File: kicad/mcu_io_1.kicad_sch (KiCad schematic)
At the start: 1 part, among them U5 MCXN947VDFT

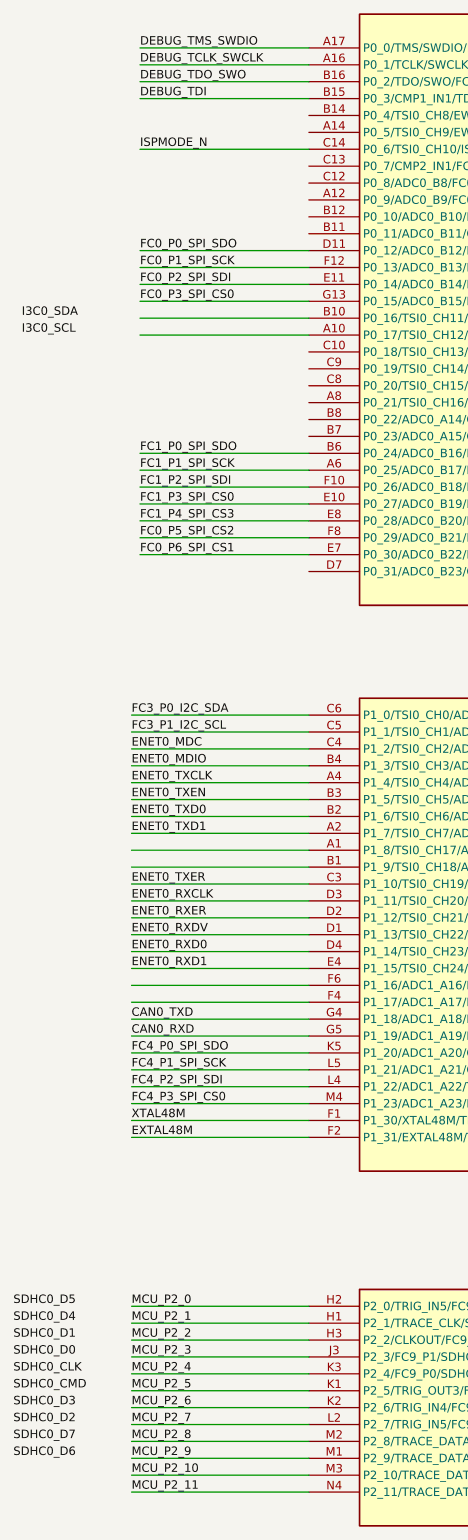
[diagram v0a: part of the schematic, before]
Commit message: Updated schematics and BOM.
- Finished power supply schematics
- Added power schematic around MCXN
- Assigned MCXN pins
- Created board-to-board schematic and assigned pins to DF40T board-to-board connector
- Added correct sensors, finished sensor schematic
- Updated parts in communication schematic
- Added all part numbers etc in parts parameters
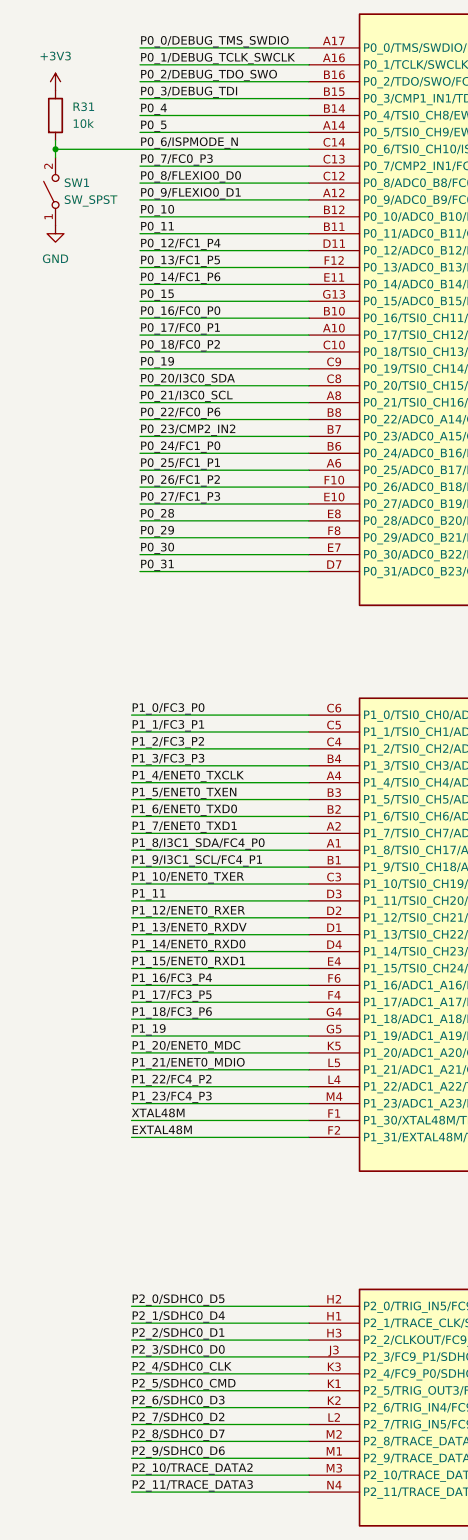
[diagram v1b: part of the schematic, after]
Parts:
- added R31: 10k, Resistor_SMD:R_0402_1005Metric, symbol Device:R
- added SW1: SW_SPST, Switches:TS2306A, symbol Switch:SW_SPST
- U5: MF (none) -> NXP USA Inc.; MFPN (none) -> MCXN947VDFT; Supplier (none) -> DigiKey; Supplier PN (none) -> 568-MCXN947VDFT-ND
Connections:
- net P0_17/FC0_P1: now reaches U5.A10 (P0_17/TSI0_CH12/ADC0_A9/FC0_P1/CT0_MAT1/UTICK_CAP3/FLEXIO0_D1/PDM0_DATA0/I3C0_SCL/TP_HREADY)
- net P0_9/FLEXIO0_D1: now reaches U5.A12 (P0_9/ADC0_B9/FC0_P5/CT_INP1/FLEXIO0_D1)
- net P0_5: now reaches U5.A14 (P0_5/TSI0_CH9/EWM0_OUT_b/FC0_P1/FC1_P5/CT0_MAT3/UTICK_CAP3/PDM0_DATA0)
- net P0_21/I3C0_SCL: now reaches U5.A8 (P0_21/TSI0_CH16/ADC0_A13/FC0_P5/FC1_P1/CT_INP1/FLEXIO0_D5/I3C0_SCL)
- net P0_16/FC0_P0: now reaches U5.B10 (P0_16/TSI0_CH11/ADC0_A8/FC0_P0/CT0_MAT0/UTICK_CAP2/FLEXIO0_D0/PDM0_CLK/I3C0_SDA/TP_HRESP/WUU0_IN2)
- net P0_11: now reaches U5.B11 (P0_11/ADC0_B11/CT0_MAT1/FLEXIO0_D3/HSCMP2_OUT)
- net P0_10: now reaches U5.B12 (P0_10/ADC0_B10/FC0_P6/CT0_MAT0/FLEXIO0_D2)
- net P0_4: now reaches U5.B14 (P0_4/TSI0_CH8/EWM0_IN/FC0_P0/FC1_P4/CT0_MAT2/UTICK_CAP2/HSCMP1_OUT/PDM0_CLK/WUU0_IN0)
- net P0_23/CMP2_IN2: now reaches U5.B7 (P0_23/ADC0_A15/CMP2_IN2/EWM0_OUT_b/FC1_P3/CT_INP3/FLEXIO0_D7/WUU0_IN5)
- net P0_22/FC0_P6: now reaches U5.B8 (P0_22/ADC0_A14/CMP1_IN2/EWM0_IN/FC0_P6/FC1_P2/CT_INP2/FLEXIO0_D6/I3C0_PUR)
- net P0_18/FC0_P2: now reaches U5.C10 (P0_18/TSI0_CH13/ADC0_A10/EWM0_IN/FC0_P2/CT0_MAT2/FLEXIO0_D2/HSCMP0_OUT/PDM0_DATA1)
- net P0_8/FLEXIO0_D0: now reaches U5.C12 (P0_8/ADC0_B8/FC0_P4/CT_INP0/FLEXIO0_D0)
- net P0_7/FC0_P3: now reaches U5.C13 (P0_7/CMP2_IN1/FC0_P3/CT_INP3/WUU0_IN1)
- net P0_20/I3C0_SDA: now reaches U5.C8 (P0_20/TSI0_CH15/ADC0_A12/FC0_P4/FC1_P0/CT_INP0/FLEXIO0_D4/I3C0_SDA/WUU0_IN4)
- net P0_19: now reaches U5.C9 (P0_19/TSI0_CH14/ADC0_A11/EWM0_OUT_b/FC0_P3/CT0_MAT3/FLEXIO0_D3/HSCMP1_OUT/WUU0_IN3)
- net P0_31: now reaches U5.D7 (P0_31/ADC0_B23/CT_INP3)
- net P1_8/I3C1_SDA/FC4_P0: now reaches U5.A1 (P1_8/TSI0_CH17/ADC1_A8/TRACE_DATA0/FC4_P0/FC5_P4/CT_INP8/SCT0_OUT2/FLEXIO0_D16/EZH_PIO4/PLU_OUT0/ENET0_TXD2/I3C1_SDA/TP_DATA0/WUU0_IN10/LPTMR1_ALT3)
- net P1_9/I3C1_SCL/FC4_P1: now reaches U5.B1 (P1_9/TSI0_CH18/ADC1_A9/TRACE_DATA1/FC4_P1/FC5_P5/CT_INP9/SCT0_OUT3/FLEXIO0_D17/EZH_PIO5/PLU_OUT1/ENET0_TXD3/I3C1_SCL/TP_DATA1)
- net P1_17/FC3_P5: now reaches U5.F4 (P1_17/ADC1_A17/FC5_P1/FC3_P5/CT_INP13/SCT0_OUT7/FLEXIO0_D25/EZH_PIO13/PLU_OUT5/ENET0_RXD3/I3C1_SCL)
- net P1_16/FC3_P4: now reaches U5.F6 (P1_16/ADC1_A16/FC5_P0/FC3_P4/CT_INP12/SCT0_OUT6/FLEXIO0_D24/EZH_PIO12/PLU_OUT4/ENET0_RXD2/I3C1_SDA/WUU0_IN14)
- net CAN0_RXD renamed P1_19
- net CAN0_TXD renamed P1_18/FC3_P6
- net DEBUG_TCLK_SWCLK renamed P0_1/DEBUG_TCLK_SWCLK
- net DEBUG_TDI renamed P0_3/DEBUG_TDI
- net DEBUG_TDO_SWO renamed P0_2/DEBUG_TDO_SWO
- net DEBUG_TMS_SWDIO renamed P0_0/DEBUG_TMS_SWDIO
- net ENET0_MDC renamed P1_2/FC3_P2
- net ENET0_MDIO renamed P1_3/FC3_P3
- net ENET0_RXCLK renamed P1_11
- net ENET0_RXD0 renamed P1_14/ENET0_RXD0
- net ENET0_RXD1 renamed P1_15/ENET0_RXD1
- net ENET0_RXDV renamed P1_13/ENET0_RXDV
- net ENET0_RXER renamed P1_12/ENET0_RXER
- net ENET0_TXCLK renamed P1_4/ENET0_TXCLK
- net ENET0_TXD0 renamed P1_6/ENET0_TXD0
- net ENET0_TXD1 renamed P1_7/ENET0_TXD1
- net ENET0_TXEN renamed P1_5/ENET0_TXEN
- net ENET0_TXER renamed P1_10/ENET0_TXER
- net FC0_P0_SPI_SDO renamed P0_12/FC1_P4
- net FC0_P1_SPI_SCK renamed P0_13/FC1_P5
- net FC0_P2_SPI_SDI renamed P0_14/FC1_P6
- net FC0_P3_SPI_CS0 renamed P0_15
- net FC0_P5_SPI_CS2 renamed P0_29
- net FC0_P6_SPI_CS1 renamed P0_30
- net FC1_P0_SPI_SDO renamed P0_24/FC1_P0
- net FC1_P1_SPI_SCK renamed P0_25/FC1_P1
- net FC1_P2_SPI_SDI renamed P0_26/FC1_P2
- net FC1_P3_SPI_CS0 renamed P0_27/FC1_P3
- net FC1_P4_SPI_CS3 renamed P0_28
- net FC3_P0_I2C_SDA renamed P1_0/FC3_P0
- net FC3_P1_I2C_SCL renamed P1_1/FC3_P1
- net FC4_P0_SPI_SDO renamed P1_20/ENET0_MDC
- net FC4_P1_SPI_SCK renamed P1_21/ENET0_MDIO
- net FC4_P2_SPI_SDI renamed P1_22/FC4_P2
- net FC4_P3_SPI_CS0 renamed P1_23/FC4_P3
- net ISPMODE_N renamed P0_6/ISPMODE_N
- net P0_6/ISPMODE_N: now also R31.2, SW1.2 (B)
- net MCU_P2_0 renamed P2_0/SDHC0_D5
- net MCU_P2_1 renamed P2_1/SDHC0_D4
- net MCU_P2_10 renamed P2_10/TRACE_DATA2
- net MCU_P2_11 renamed P2_11/TRACE_DATA3
- net MCU_P2_2 renamed P2_2/SDHC0_D1
- net MCU_P2_3 renamed P2_3/SDHC0_D0
- net MCU_P2_4 renamed P2_4/SDHC0_CLK
- net MCU_P2_5 renamed P2_5/SDHC0_CMD
- net MCU_P2_6 renamed P2_6/SDHC0_D3
- net MCU_P2_7 renamed P2_7/SDHC0_D2
- net MCU_P2_8 renamed P2_8/SDHC0_D7
- net MCU_P2_9 renamed P2_9/SDHC0_D6
- new net +3V3: R31.1
- new net GND: SW1.1 (A)

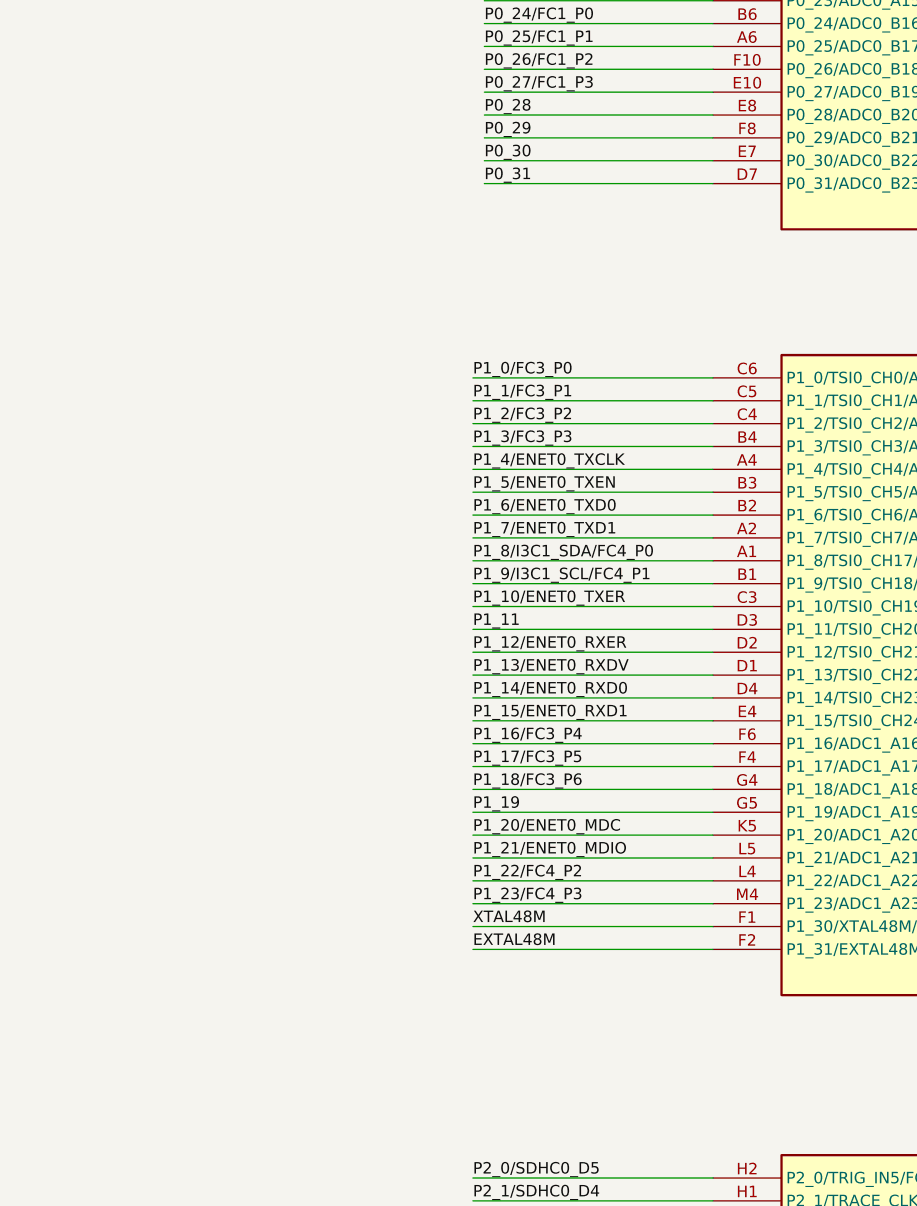
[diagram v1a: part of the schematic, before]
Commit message: Finished schematic design for first review
Finished schematic design for first review.
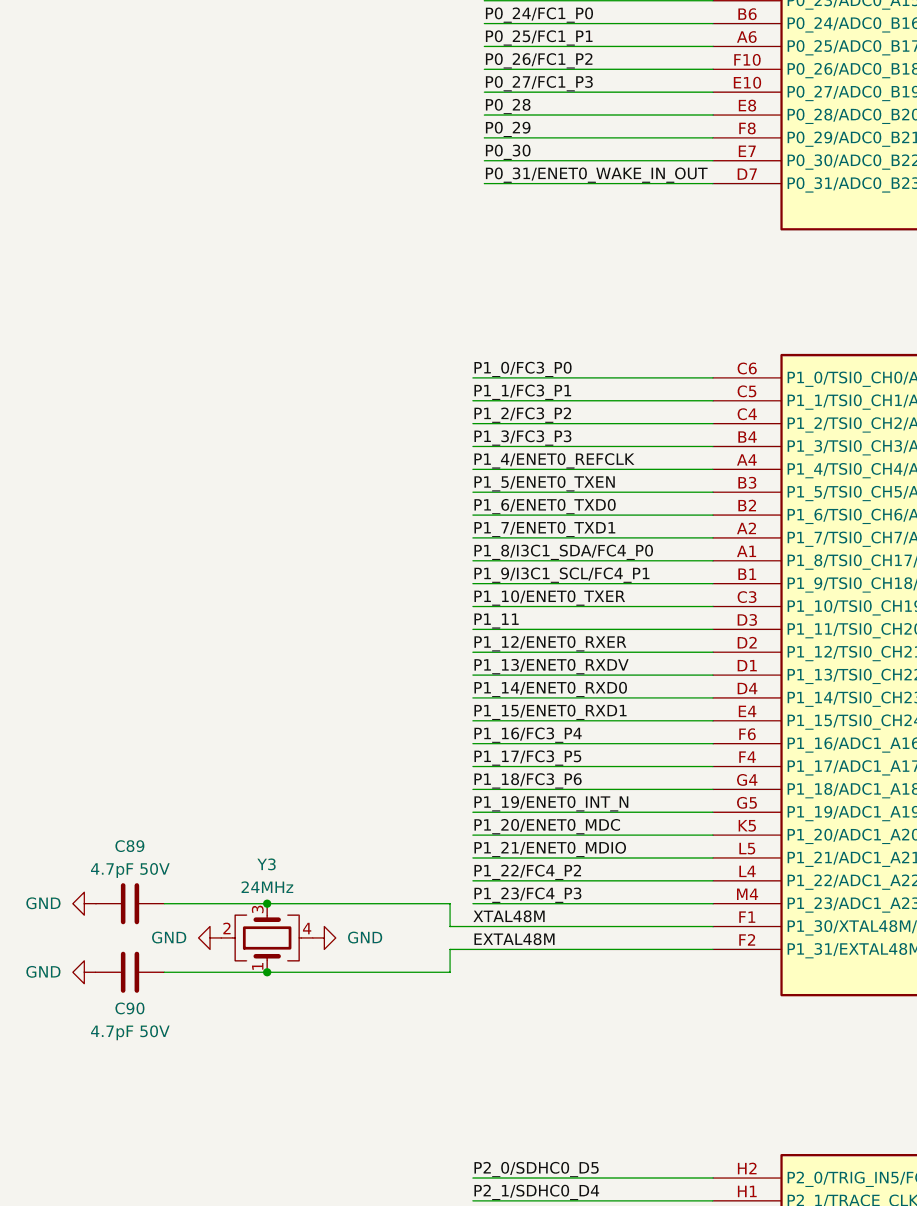
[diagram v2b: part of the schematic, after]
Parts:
- added C89, C90: 4.7pF 50V, Capacitor_SMD:C_0402_1005Metric, symbol Device:C
- added Y3: 24MHz, Crystal:Crystal_SMD_2016-4Pin_2.0x1.6mm, symbol Device:Crystal_GND24
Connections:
- net EXTAL48M: now also C90.2, Y3.1
- net GND: now also C89.1, C90.1, Y3.2, Y3.4
- net XTAL48M: now also C89.2, Y3.3
- net P0_31 renamed P0_31/ENET0_WAKE_IN_OUT
- net P1_19 renamed P1_19/ENET0_INT_N
- net P1_4/ENET0_TXCLK renamed P1_4/ENET0_REFCLK

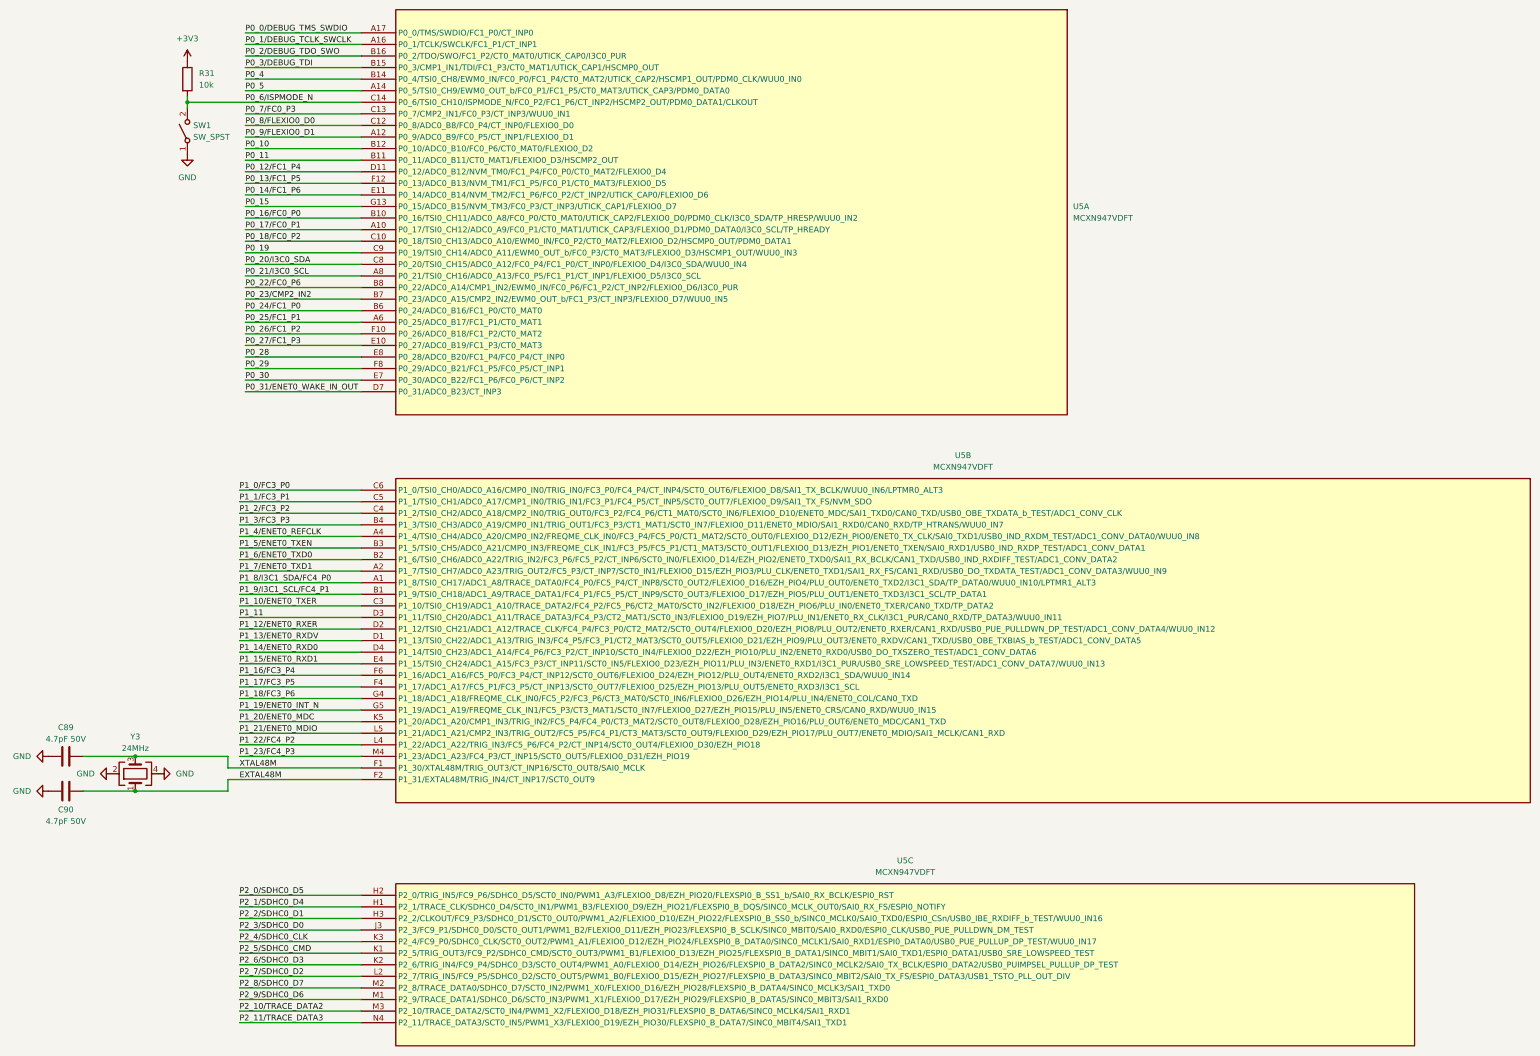
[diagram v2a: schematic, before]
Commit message: Updated schematic and started on layout
- Implemented schematic changes after feedback:
	- BMM350 VDD is 1.8V
	- Replaced net labels with global labels for page references
	- Added 1uF cap to SK9822-EC20
- Added rev-RMII configuration for TJA1103 and DNP resistor to put it in slave mode
- Added TJA1103 PHY address info
- Changed decoupling caps for MCXN to smallest possible packages
- Added traces and vias at MCXN according to guidelines
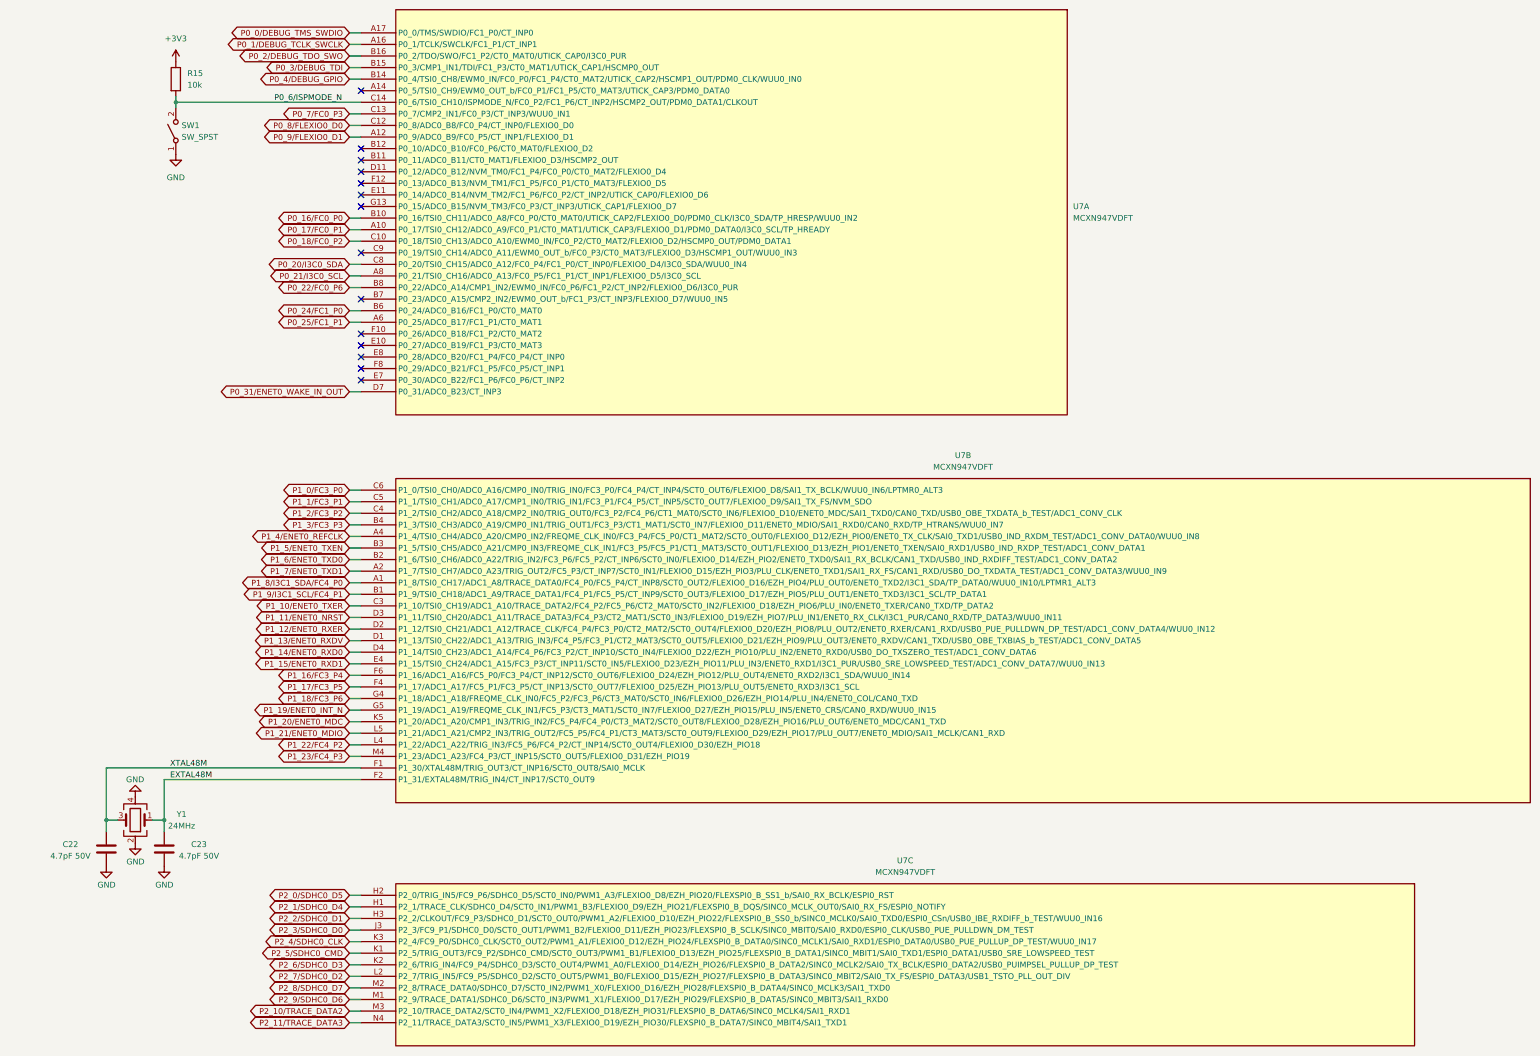
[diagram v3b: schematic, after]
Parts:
- renumbered C89 to C22, C90 to C23, R31 to R15, U5 to U7, Y3 to Y1
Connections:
- net P0_10: no longer names the net of U7.B12 (P0_10/ADC0_B10/FC0_P6/CT0_MAT0/FLEXIO0_D2)
- net P0_11: no longer names the net of U7.B11 (P0_11/ADC0_B11/CT0_MAT1/FLEXIO0_D3/HSCMP2_OUT)
- net P0_12/FC1_P4: no longer names the net of U7.D11 (P0_12/ADC0_B12/NVM_TM0/FC1_P4/FC0_P0/CT0_MAT2/FLEXIO0_D4)
- net P0_13/FC1_P5: no longer names the net of U7.F12 (P0_13/ADC0_B13/NVM_TM1/FC1_P5/FC0_P1/CT0_MAT3/FLEXIO0_D5)
- net P0_14/FC1_P6: no longer names the net of U7.E11 (P0_14/ADC0_B14/NVM_TM2/FC1_P6/FC0_P2/CT_INP2/UTICK_CAP0/FLEXIO0_D6)
- net P0_15: no longer names the net of U7.G13 (P0_15/ADC0_B15/NVM_TM3/FC0_P3/CT_INP3/UTICK_CAP1/FLEXIO0_D7)
- net P0_19: no longer names the net of U7.C9 (P0_19/TSI0_CH14/ADC0_A11/EWM0_OUT_b/FC0_P3/CT0_MAT3/FLEXIO0_D3/HSCMP1_OUT/WUU0_IN3)
- net P0_23/CMP2_IN2: no longer names the net of U7.B7 (P0_23/ADC0_A15/CMP2_IN2/EWM0_OUT_b/FC1_P3/CT_INP3/FLEXIO0_D7/WUU0_IN5)
- net P0_26/FC1_P2: no longer names the net of U7.F10 (P0_26/ADC0_B18/FC1_P2/CT0_MAT2)
- net P0_27/FC1_P3: no longer names the net of U7.E10 (P0_27/ADC0_B19/FC1_P3/CT0_MAT3)
- net P0_28: no longer names the net of U7.E8 (P0_28/ADC0_B20/FC1_P4/FC0_P4/CT_INP0)
- net P0_29: no longer names the net of U7.F8 (P0_29/ADC0_B21/FC1_P5/FC0_P5/CT_INP1)
- net P0_30: no longer names the net of U7.E7 (P0_30/ADC0_B22/FC1_P6/FC0_P6/CT_INP2)
- net P0_4 renamed P0_4/DEBUG_GPIO
- net P0_5: no longer names the net of U7.A14 (P0_5/TSI0_CH9/EWM0_OUT_b/FC0_P1/FC1_P5/CT0_MAT3/UTICK_CAP3/PDM0_DATA0)
- net P1_11 renamed P1_11/ENET0_NRST
- no-connect marks 0 -> 14
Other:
- moved on the sheet: C22, C23, R15, SW1, Y1
